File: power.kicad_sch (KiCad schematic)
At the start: 25 parts

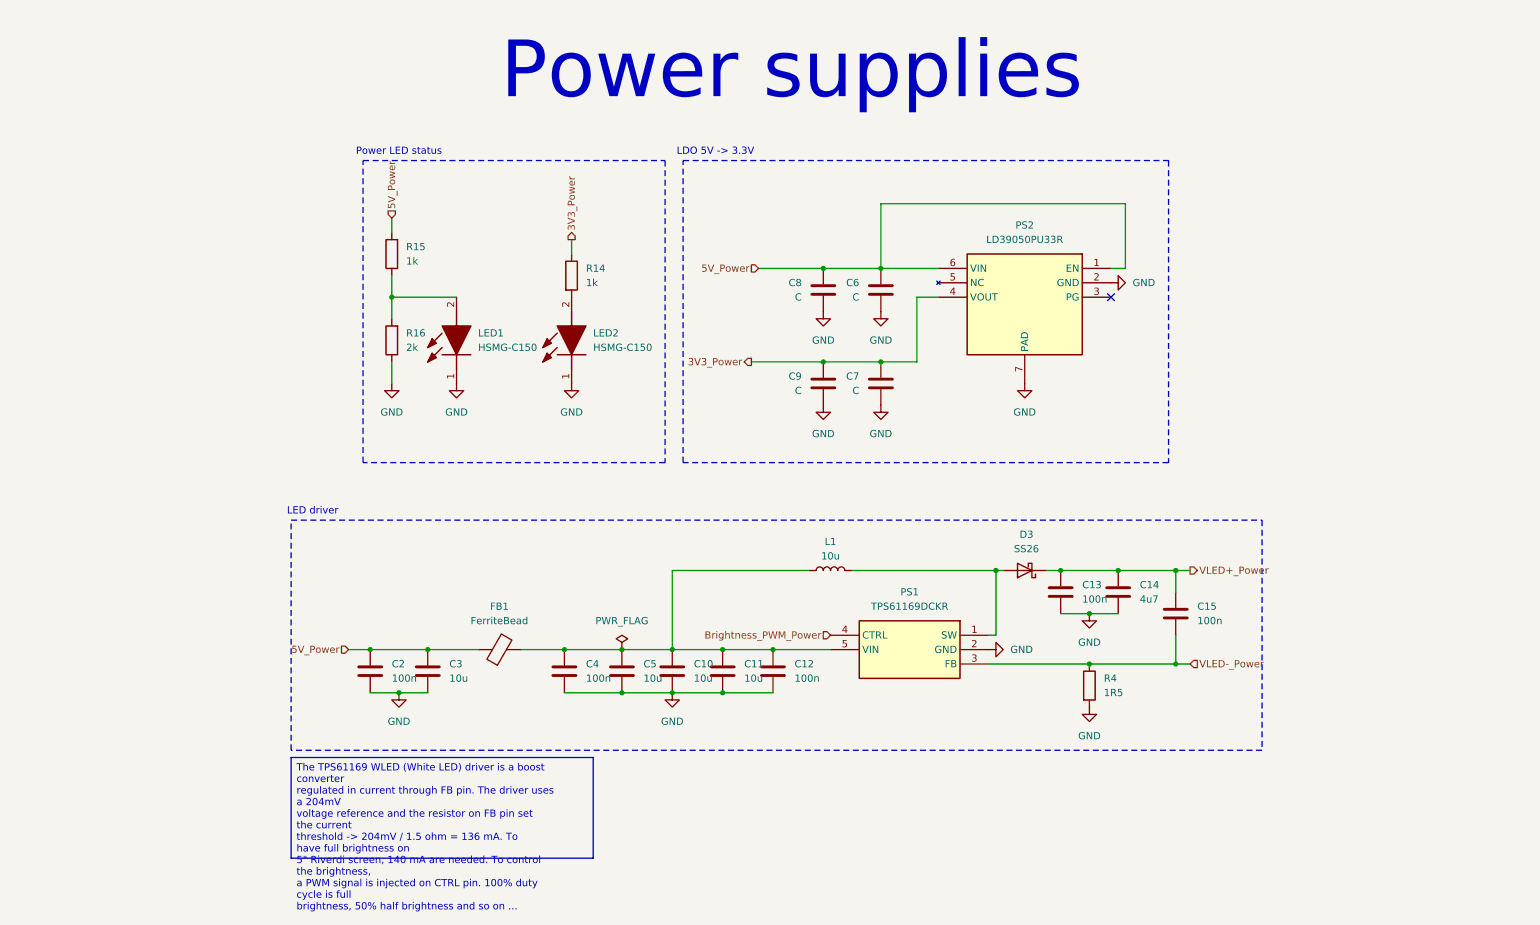
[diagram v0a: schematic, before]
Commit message: Finish ethernet schematic and add second LDO for wake/sleep of ETH
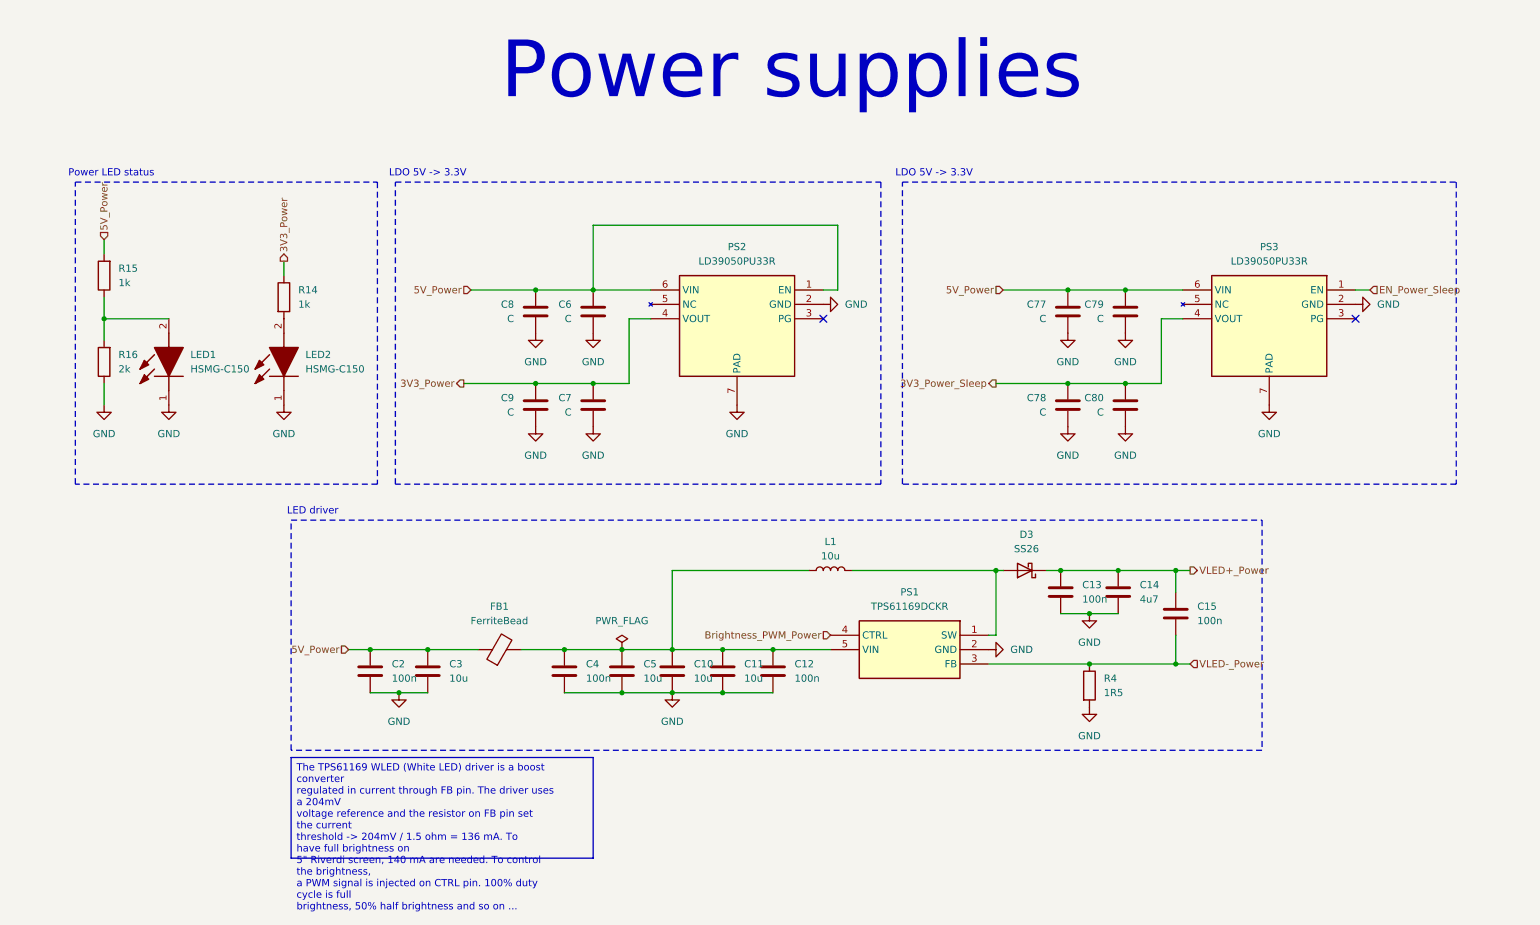
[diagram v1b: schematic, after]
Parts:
- added C77, C78, C79, C80: C, Capacitor_SMD:C_0603_1608Metric_Pad1.08x0.95mm_HandSolder, symbol Device:C
- added PS3: LD39050PU33R, weather-station-poc-fp:SON95P300X300X100-7N-D, symbol weather-station-poc-sym:LD39050PU33R
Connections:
- net 5V_Power: now also C77.1, C79.1, PS3.6 (VIN)
- net GND: now also C77.2, C78.2, C79.2, C80.2, PS3.2 (GND), PS3.7 (PAD)
- new net 3V3_Power_Sleep: C78.1, C80.1, PS3.4 (VOUT)
- new net EN_Power_Sleep: PS3.1 (EN)
- no-connect marks 1 -> 2
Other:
- moved on the sheet: C6, C7, C8, C9, LED1, LED2, PS2, R14, R15, R16

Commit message: Reorganise synoptic schematic for better reading Closes #26
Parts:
- LED1, LED2: footprint LEDC3216X120N -> weather-station-poc-fp:LEDC3216X120N
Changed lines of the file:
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@@
 			)
 		)
-		(property "Footprint" "LEDC3216X120N"
+		(property "Footprint" "weather-station-poc-fp:LEDC3216X120N"
 			(at 136.83 69.85 0)
 			(effects
@@
 			)
 		)
-		(property "Footprint" "LEDC3216X120N"
+		(property "Footprint" "weather-station-poc-fp:LEDC3216X120N"
 			(at 157.15 69.85 0)
 			(effects

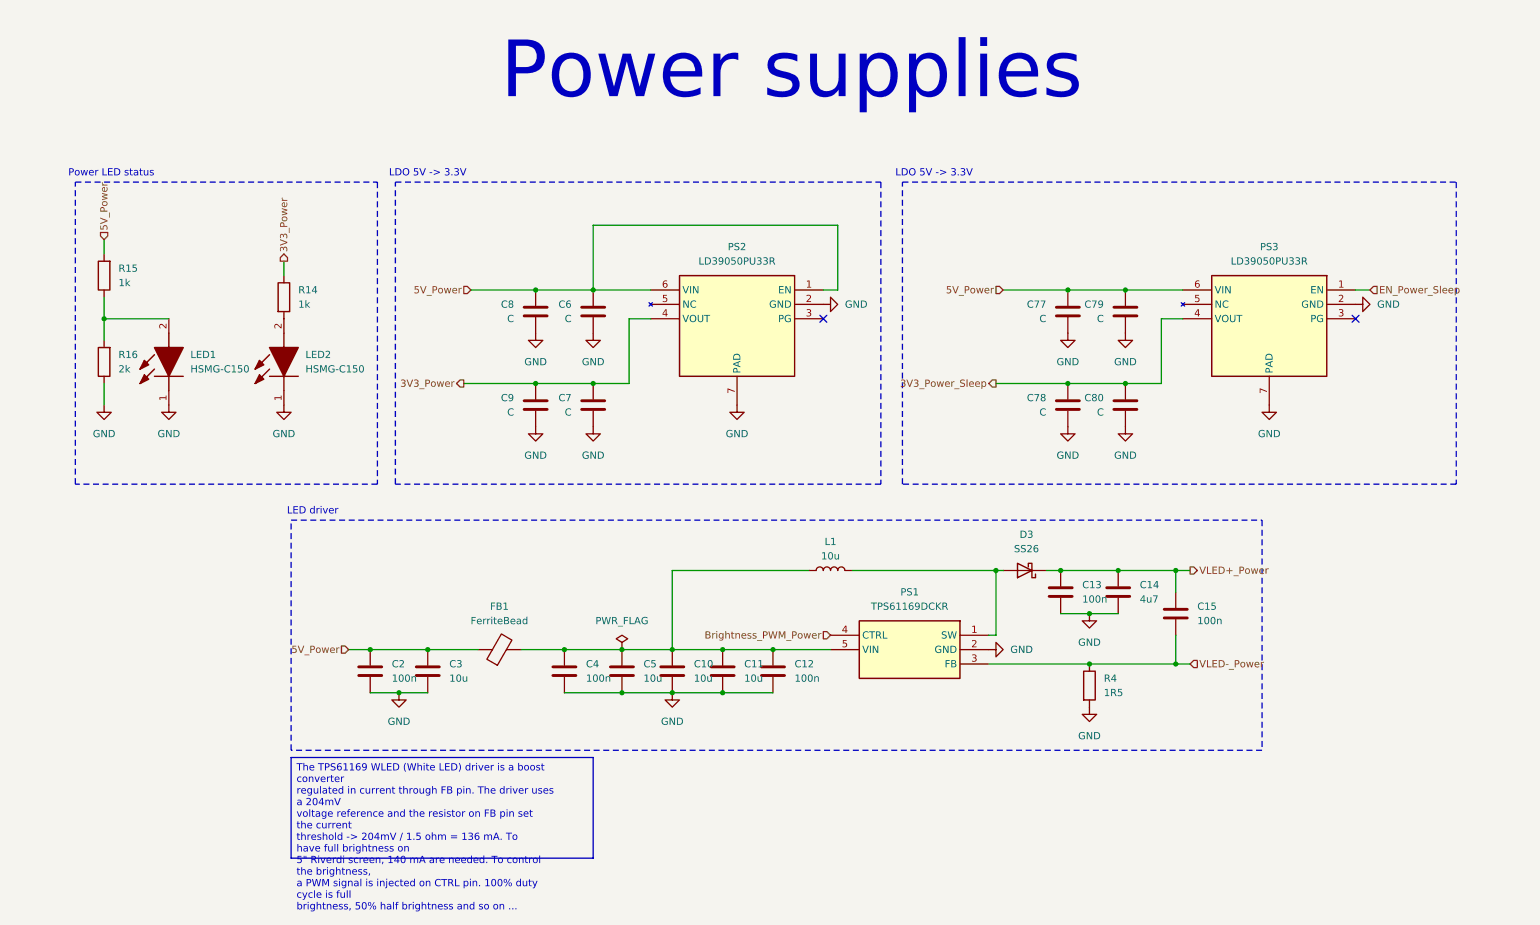
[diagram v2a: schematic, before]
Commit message: Fix errors in synoptic and hierarchic pins
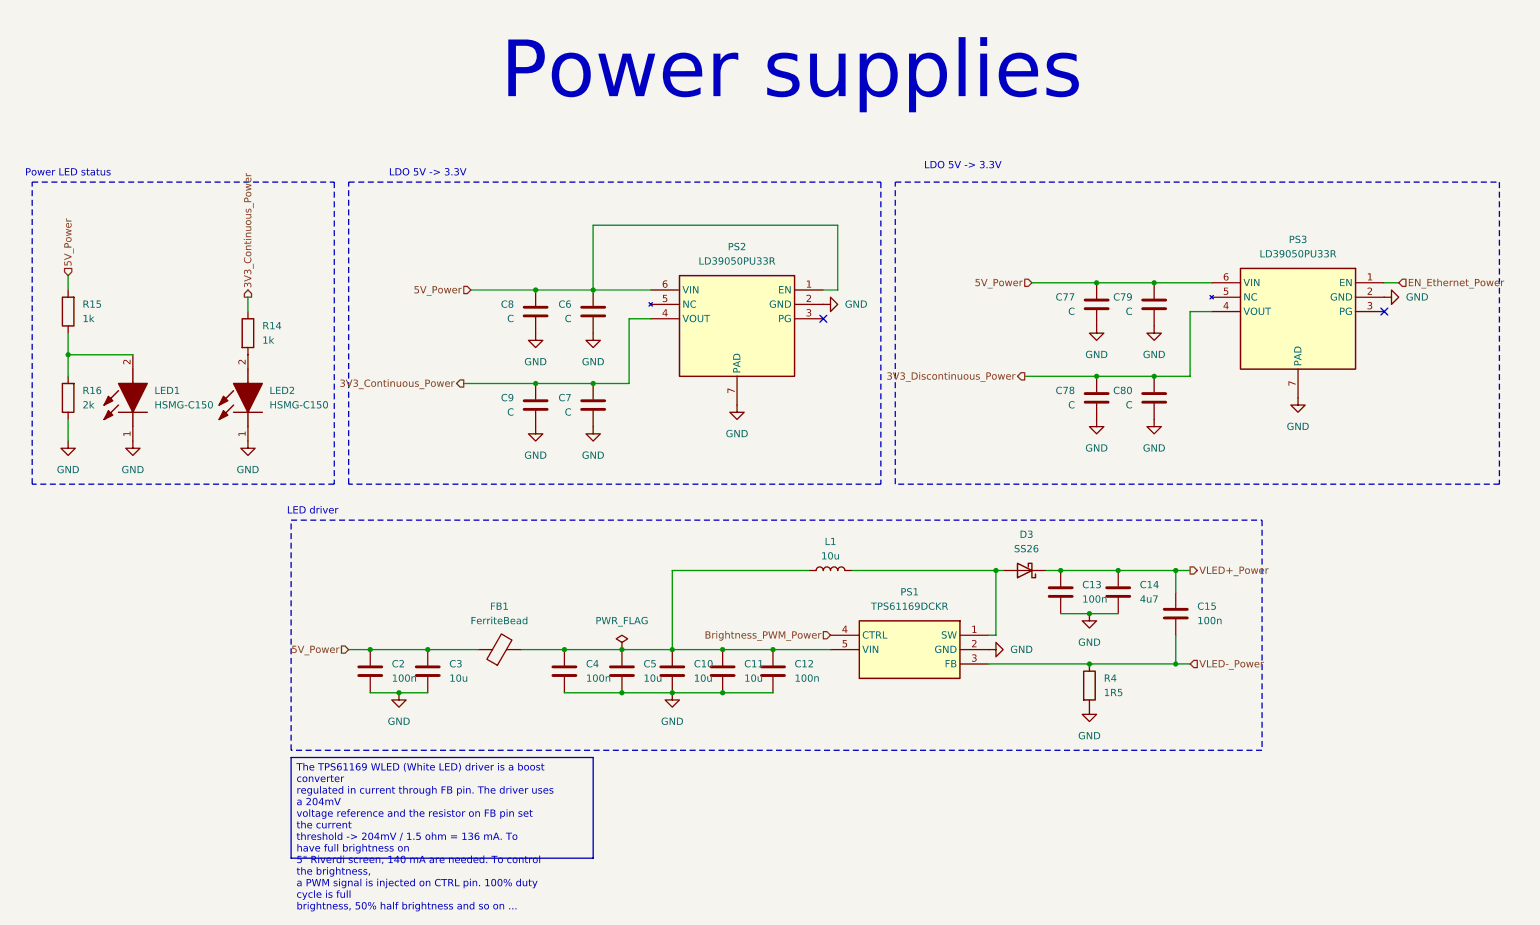
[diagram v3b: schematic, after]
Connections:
- net 3V3_Power renamed 3V3_Continuous_Power
- net 3V3_Power_Sleep renamed 3V3_Discontinuous_Power
- net EN_Power_Sleep renamed EN_Ethernet_Power
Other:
- moved on the sheet: C77, C78, C79, C80, LED1, LED2, PS3, R14, R15, R16

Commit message: Continue schematic review
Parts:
- removed C80: C, Capacitor_SMD:C_0603_1608Metric_Pad1.08x0.95mm_HandSolder, symbol Device:C
- added C60: 1u, symbol Device:C
- added LED4: HSMG-C150, weather-station-poc-fp:LEDC3216X120N, symbol weather-station-poc-sym:HSMG-C150
- added R24: 1k, symbol Device:R
- C6, C78, C8: value C -> 1u; footprint Capacitor_SMD:C_0603_1608Metric_Pad1.08x0.95mm_HandSolder -> (none)
- C7, C77, C79, C9: value C -> 100n; footprint Capacitor_SMD:C_0603_1608Metric_Pad1.08x0.95mm_HandSolder -> (none)
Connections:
- net 3V3_Continuous_Power: now also C8.1; no longer C7.1
- net 3V3_Discontinuous_Power: now also C79.1, R24.1
- net 5V_Power: now also C7.1, C60.1; no longer C79.1, C8.1
- net GND: now also C60.2, LED4.1 (K)
- new net: LED4.2 (A), R24.2
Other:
- moved on the sheet: C10, C11, C12, C13, C14, C15, C2, C3, C4, C5, D3, FB1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

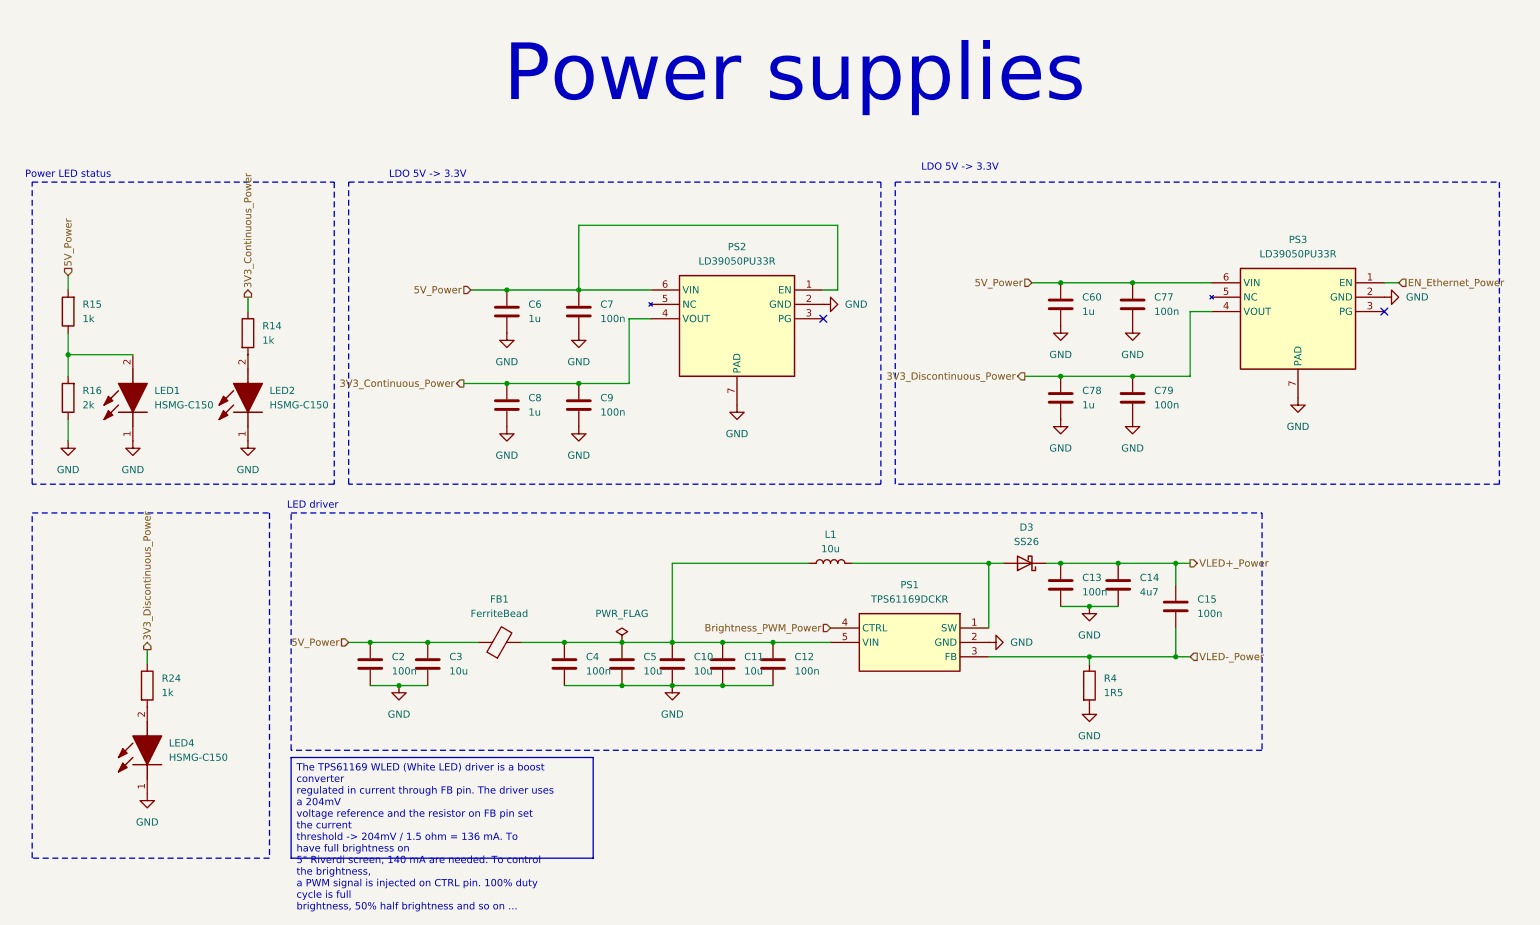
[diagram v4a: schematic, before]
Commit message: Fix some little warnings and refomat schematics files
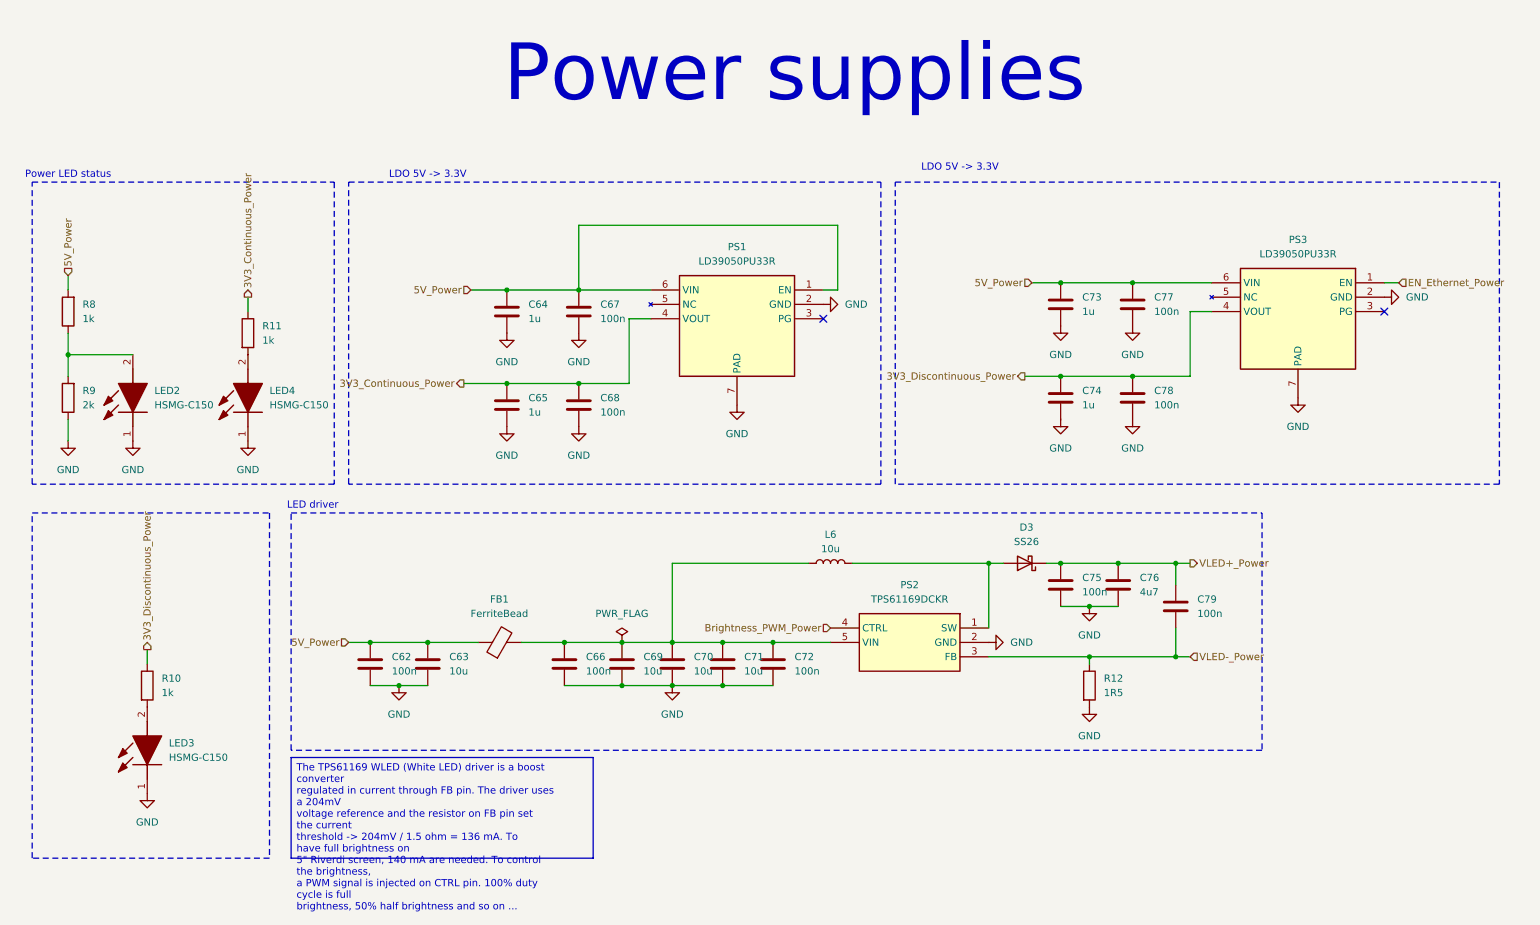
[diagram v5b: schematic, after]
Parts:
- renumbered C2 to C62, C3 to C63, C6 to C64, C8 to C65, C4 to C66, C7 to C67, C9 to C68, C5 to C69, C10 to C70, C11 to C71, C12 to C72, C60 to C73, C78 to C74, C13 to C75, C14 to C76, C79 to C78, C15 to C79, L1 to L6, LED1 to LED2, LED4 to LED3, LED2 to LED4, PS2 to PS1, PS1 to PS2, R24 to R10, R14 to R11, R4 to R12, R15 to R8, R16 to R9
